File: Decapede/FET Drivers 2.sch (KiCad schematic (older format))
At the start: 20 parts, among them J23 FET5, J24 FET5_PWM, Q29 BC817-25,215, Q30 PSMN023-40YLCX, Q31 BC807,215, Q32 BC817-25,215, Q33 PSMN023-40YLCX, Q34 BC807,215

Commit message: Updates for Decapede project.
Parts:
- removed D13, D14: Diode 10TQ035, ~, symbol DIODESCH
- added D22, D24: LED, ~, symbol LED
- added D23, D25: ES1D, ~, symbol DIODESCH
- J24: value FET5_PWM -> FET10
- Q30, Q33: symbol BUK7226-75A -> PSMN023-40YLCX
- R103, R108: value 30 Ohm -> 1k8
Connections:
- net +12V: now also R103.1, R108.1
- net +24V: now also D23.2 (K), D25.2 (K)
- net FET5: now also R105.1
- net FET5_PWM: now also R110.1
- net GND: now also Q30.1 (S), Q33.1 (S); no longer Q30.3 (S), Q33.3 (S)
- net at Q31.2 (E), R104.2: no longer R103.2
- net FET_OUT_5: now reaches J23.2 (PM)
- net FET_OUT_5: now also Q30.5 (D), D22.2 (K), D23.1 (A); no longer Q30.2 (D)
- net at Q34.2 (E), R109.2: no longer R108.2
- net FET_OUT_P5: now reaches J24.2 (PM)
- net FET_OUT_P5: now also Q33.5 (D), D24.2 (K), D25.1 (A); no longer Q33.2 (D)
- new net: Q30.4 (G), R101.2, R104.1
- new net: Q33.4 (G), R107.2, R109.1
- new net: D24.1 (A), R108.2
- new net: D22.1 (A), R103.2
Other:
- moved on the sheet: J24, Q32, Q33, Q34, R105, R106, R107, R109, R110

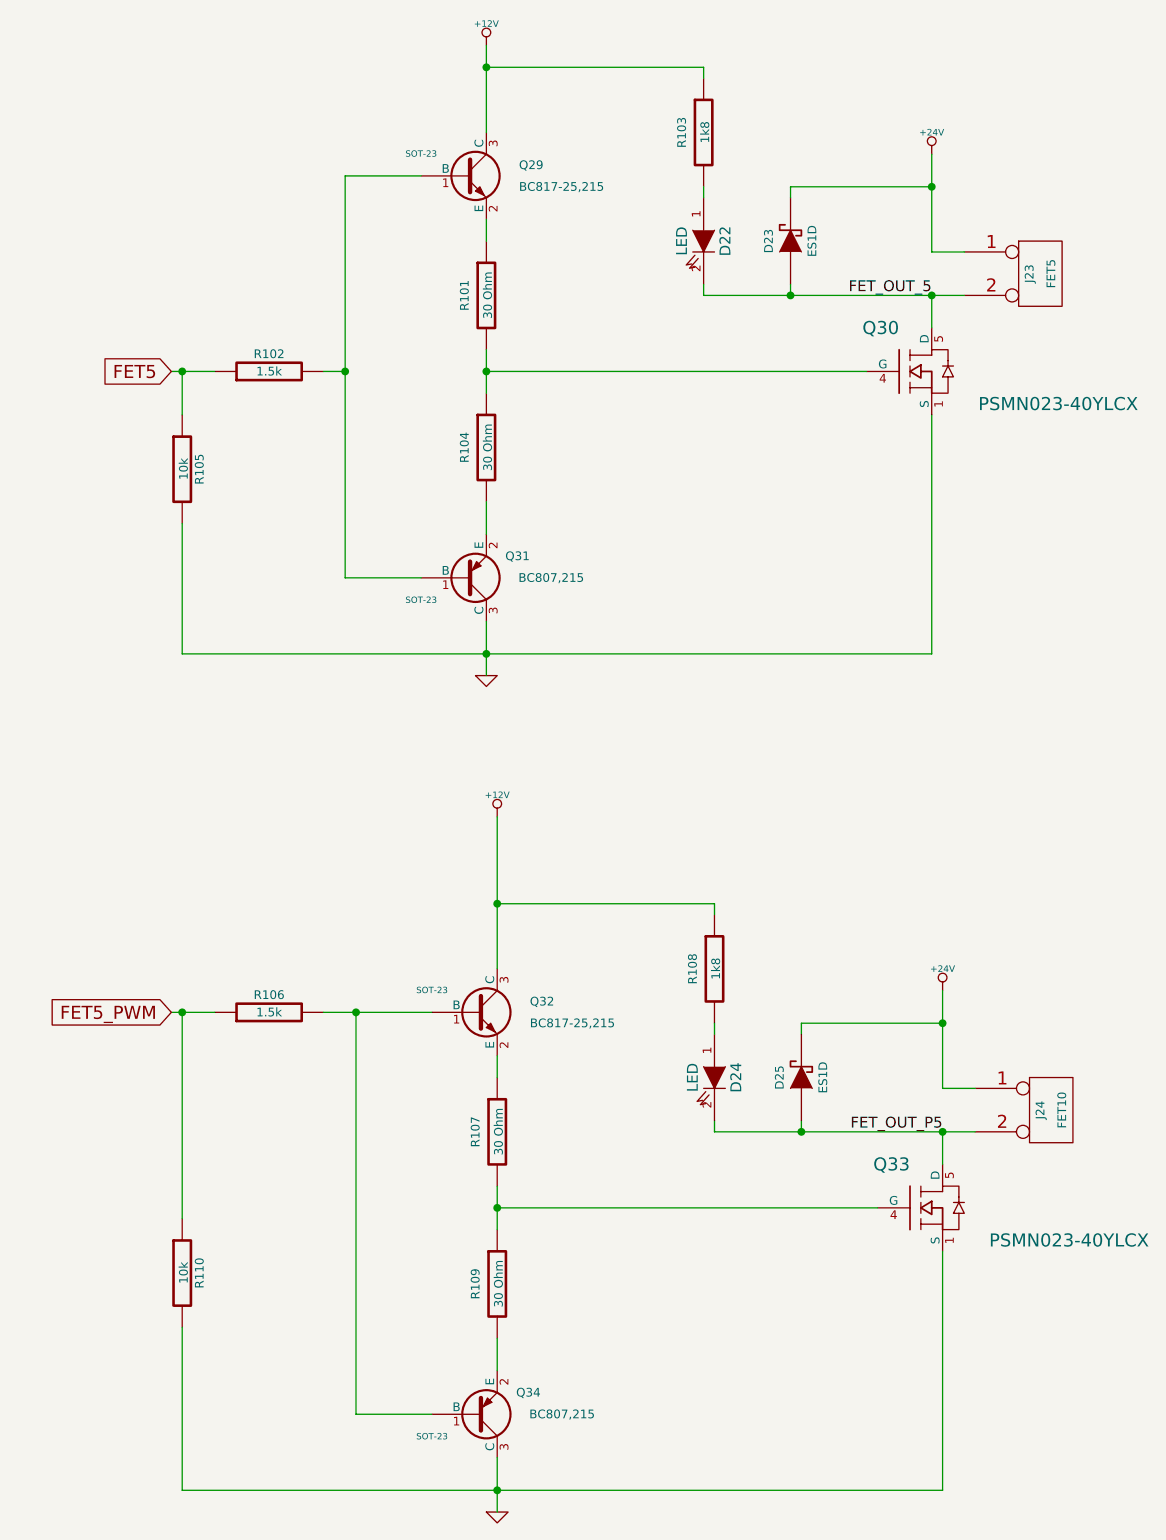
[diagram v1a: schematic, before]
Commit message: Decapede update: add fuses for each main section; change endstops to use 0V instead of 5V; more space for stepper drivers to allow latching connectors
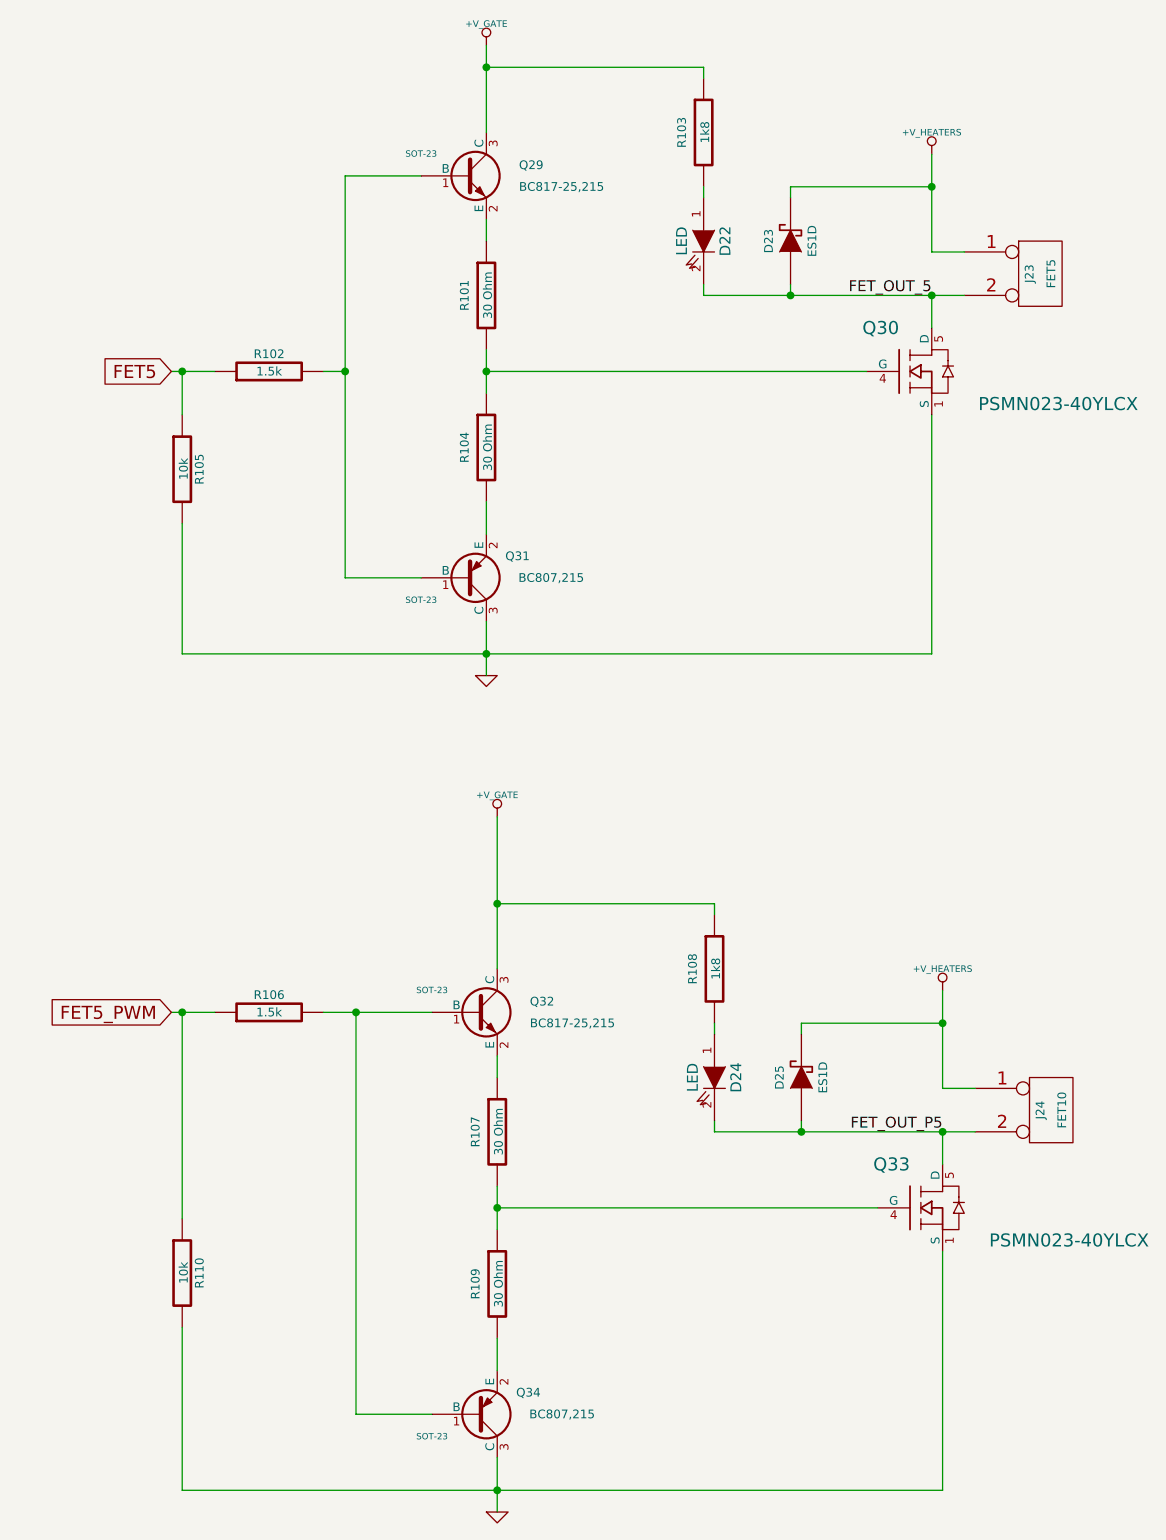
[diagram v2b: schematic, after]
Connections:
- net +12V renamed +V_GATE
- net +24V renamed +V_HEATERS
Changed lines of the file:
@@
 Sheet 9 10
 Title "FET5 Driver Stage"
-Date "26 jan 2014"
+Date "30 jan 2014"
 Rev ""
 Comp ""
@@
 $EndComp
 $Comp
-L +12V #PWR0166
-U 1 1 52DC3812
-P 2500 700
-F 0 "#PWR0166" H 2500 650 20  0001 C CNN
-F 1 "+12V" H 2500 800 30  0000 C CNN
-F 2 "" H 2500 700 60  0000 C CNN
-F 3 "" H 2500 700 60  0000 C CNN
-	1    2500 700
-	1    0    0    -1
-$EndComp
-$Comp
-L GND #PWR0167
+L GND #PWR0170
 U 1 1 52DC3818
 P 2500 3600
-F 0 "#PWR0167" H 2500 3600 30  0001 C CNN
+F 0 "#PWR0170" H 2500 3600 30  0001 C CNN
 F 1 "GND" H 2500 3530 30  0001 C CNN
 F 2 "" H 2500 3600 60  0000 C CNN
@@
 F 3 "" H 5050 1750 60  0000 C CNN
 	1    5050 1750
-	1    0    0    -1
-$EndComp
-$Comp
-L +24V #PWR0168
-U 1 1 52DC384C
-P 4550 1200
-F 0 "#PWR0168" H 4550 1150 20  0001 C CNN
-F 1 "+24V" H 4550 1300 30  0000 C CNN
-F 2 "" H 4550 1200 60  0000 C CNN
-F 3 "" H 4550 1200 60  0000 C CNN
-	1    4550 1200
 	1    0    0    -1
 $EndComp
@@
 $EndComp
 $Comp
-L +12V #PWR0169
-U 1 1 52DC3CFB
-P 2550 4250
-F 0 "#PWR0169" H 2550 4200 20  0001 C CNN
-F 1 "+12V" H 2550 4350 30  0000 C CNN
-F 2 "" H 2550 4250 60  0000 C CNN
-F 3 "" H 2550 4250 60  0000 C CNN
-	1    2550 4250
-	1    0    0    -1
-$EndComp
-$Comp
-L GND #PWR0170
+L GND #PWR0171
 U 1 1 52DC3D01
 P 2550 7450
-F 0 "#PWR0170" H 2550 7450 30  0001 C CNN
+F 0 "#PWR0171" H 2550 7450 30  0001 C CNN
 F 1 "GND" H 2550 7380 30  0001 C CNN
 F 2 "" H 2550 7450 60  0000 C CNN
@@
 F 3 "" H 5100 5600 60  0000 C CNN
 	1    5100 5600
-	1    0    0    -1
-$EndComp
-$Comp
-L +24V #PWR0171
-U 1 1 52DC3D35
-P 4600 5050
-F 0 "#PWR0171" H 4600 5000 20  0001 C CNN
-F 1 "+24V" H 4600 5150 30  0000 C CNN
-F 2 "" H 4600 5050 60  0000 C CNN
-F 3 "" H 4600 5050 60  0000 C CNN
-	1    4600 5050
 	1    0    0    -1
 $EndComp
@@
 Connection ~ 2550 4650
 Connection ~ 4600 5700
+$Comp
+L +V_GATE #PWR0172
+U 1 1 52E83791
+P 2500 700
+F 0 "#PWR0172" H 2500 670 30  0001 C CNN
+F 1 "+V_GATE" H 2500 800 30  0000 C CNN
+F 2 "~" H 2500 700 60  0000 C CNN
+F 3 "~" H 2500 700 60  0000 C CNN
+	1    2500 700
+	1    0    0    -1
+$EndComp
+$Comp
+L +V_GATE #PWR0173
+U 1 1 52E837A0
+P 2550 4250
+F 0 "#PWR0173" H 2550 4220 30  0001 C CNN
+F 1 "+V_GATE" H 2550 4350 30  0000 C CNN
+F 2 "~" H 2550 4250 60  0000 C CNN
+F 3 "~" H 2550 4250 60  0000 C CNN
+	1    2550 4250
+	1    0    0    -1
+$EndComp
+$Comp
+L +V_HEATERS #PWR0174
+U 1 1 52E837AF
+P 4600 5050
+F 0 "#PWR0174" H 4600 5020 30  0001 C CNN
+F 1 "+V_HEATERS" H 4600 5150 30  0000 C CNN
+F 2 "~" H 4600 5050 60  0000 C CNN
+F 3 "~" H 4600 5050 60  0000 C CNN
+	1    4600 5050
+	1    0    0    -1
+$EndComp
+$Comp
+L +V_HEATERS #PWR0175
+U 1 1 52E837BE
+P 4550 1200
+F 0 "#PWR0175" H 4550 1170 30  0001 C CNN
+F 1 "+V_HEATERS" H 4550 1300 30  0000 C CNN
+F 2 "~" H 4550 1200 60  0000 C CNN
+F 3 "~" H 4550 1200 60  0000 C CNN
+	1    4550 1200
+	1    0    0    -1
+$EndComp
 $EndSCHEMATC
